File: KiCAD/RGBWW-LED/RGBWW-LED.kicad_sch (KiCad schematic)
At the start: 2 parts, among them J1 Conn_01x04, J2 Conn_01x04

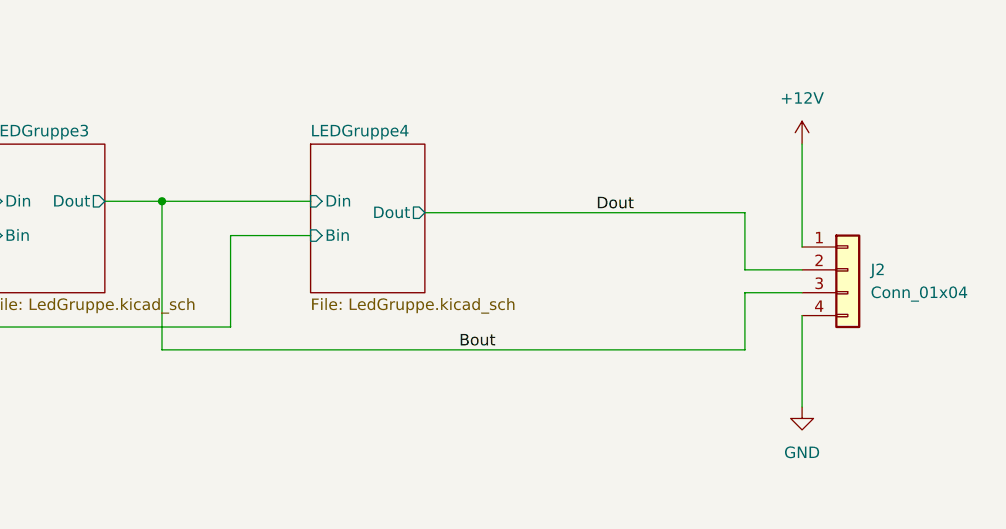
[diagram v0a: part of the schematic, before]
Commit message: Some LED groups and terminating resistor added
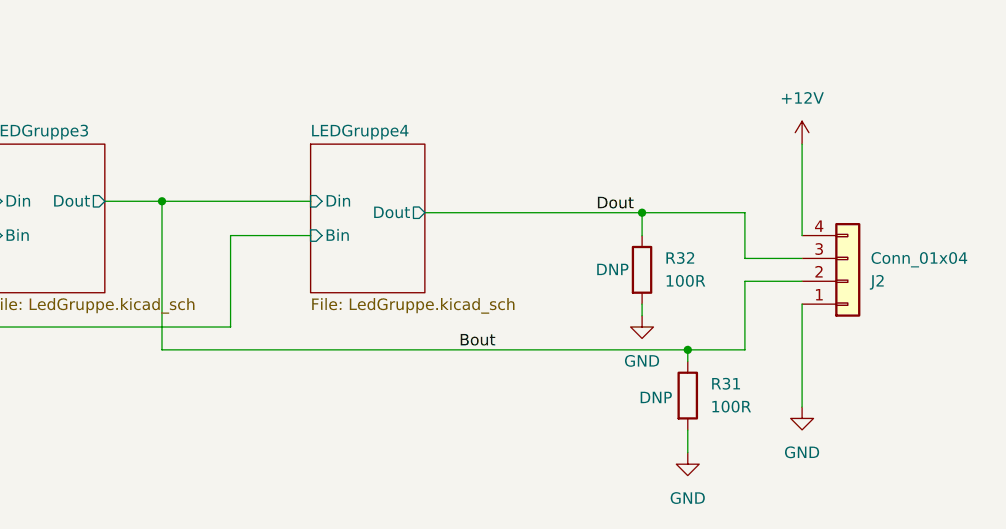
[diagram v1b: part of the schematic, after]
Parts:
- added R31, R32: 100R, Resistor_SMD:R_0603_1608Metric, symbol Device:R
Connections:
- net +12V: now also J2.4 (Pin_4); no longer J2.1 (Pin_1)
- net Bout: now also J2.2 (Pin_2), R31.1; no longer J2.3 (Pin_3)
- net Dout: now also J2.3 (Pin_3), R32.1; no longer J2.2 (Pin_2)
- net GND: now also J2.1 (Pin_1), R31.2, R32.2; no longer J2.4 (Pin_4)

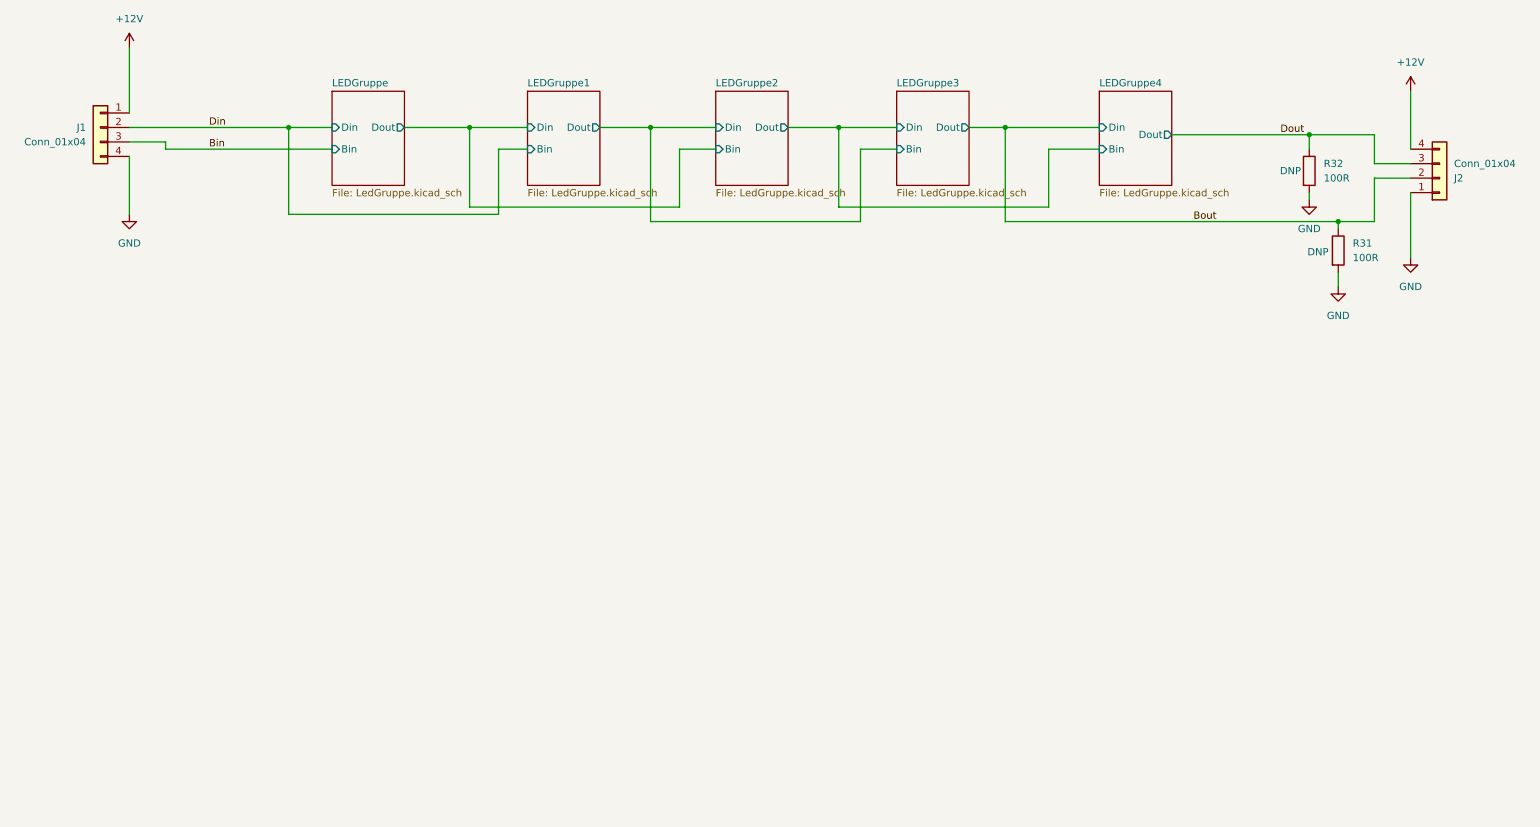
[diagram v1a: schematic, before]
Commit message: added some datasheet and started controller
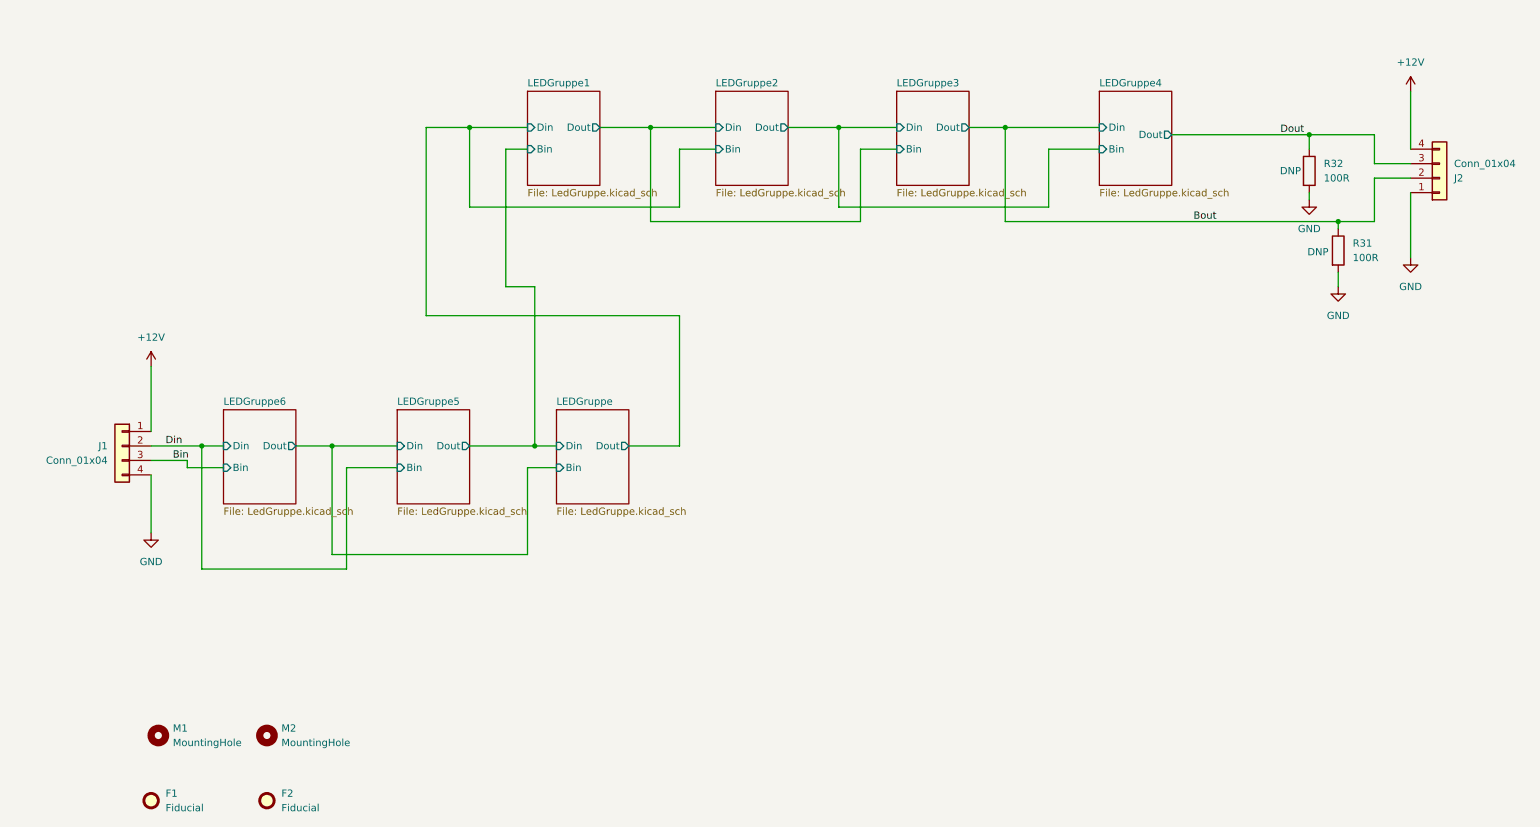
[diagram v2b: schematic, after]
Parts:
- added F1, F2: Fiducial, Fiducial:Fiducial_1mm_Mask2mm, symbol Mechanical:Fiducial
- added M1, M2: MountingHole, MountingHole:MountingHole_2.2mm_M2, symbol Mechanical:MountingHole
- R31, R32: footprint Resistor_SMD:R_0603_1608Metric -> LEDandDriver:R_0603_1608Metric_LedPrj
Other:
- added sheet LEDGruppe5 (LedGruppe.kicad_sch)
- added sheet LEDGruppe6 (LedGruppe.kicad_sch)
- moved on the sheet: J1

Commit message: longer LED board
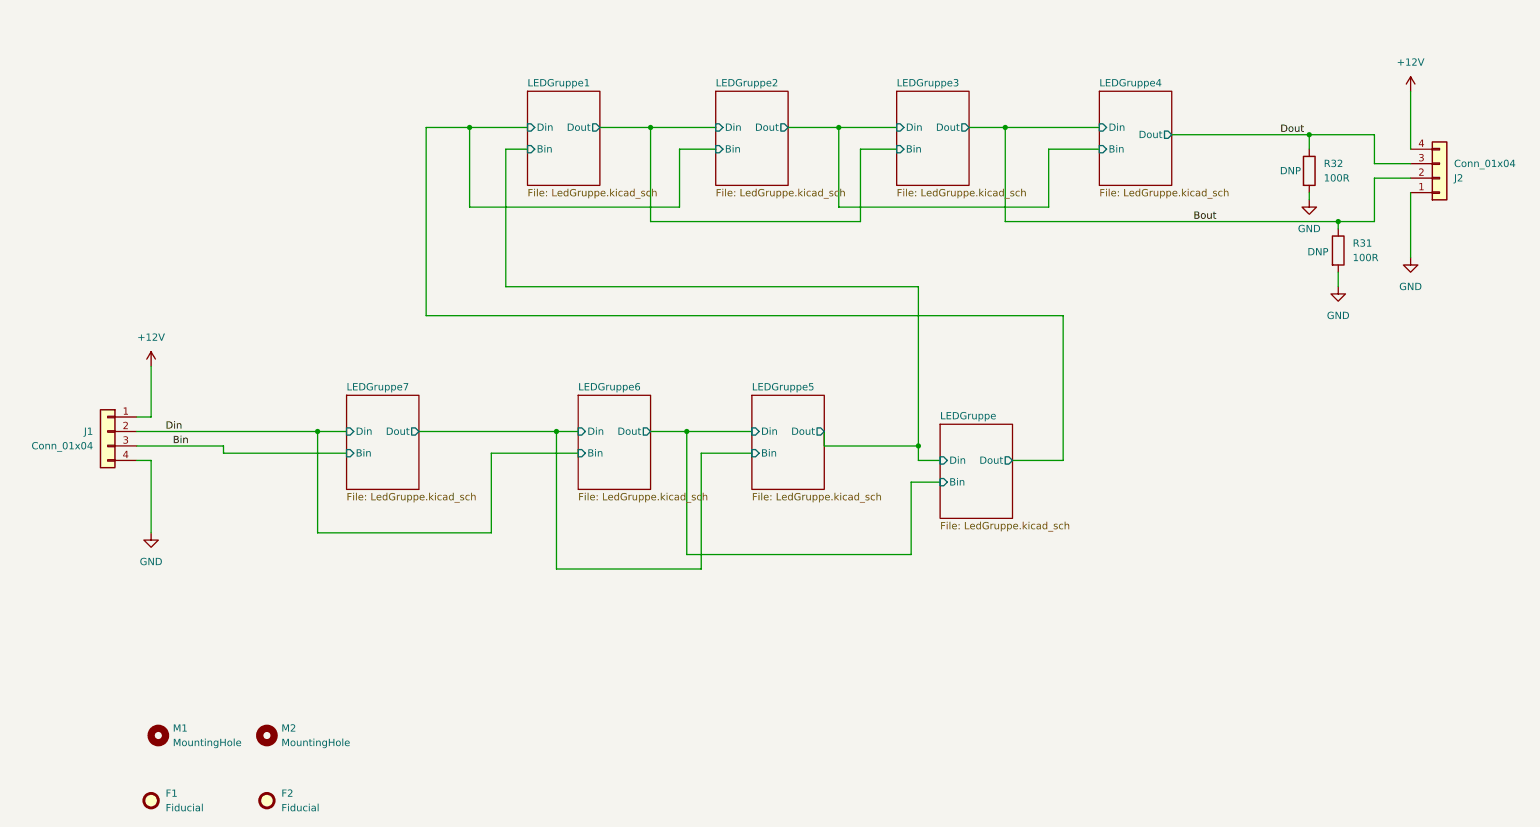
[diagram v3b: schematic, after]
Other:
- added sheet LEDGruppe7 (LedGruppe.kicad_sch)
- moved on the sheet: J1
